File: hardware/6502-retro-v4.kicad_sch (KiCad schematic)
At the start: 51 parts, among them J1 SDCARD, J2 SPI BUS, J3 GPIO, J4 CTS, J5 RTS, J6 UART, J7 JOY1, J8 SPK/AMP, J9 USB-C Adapter, U1 W65C22NxP, U10 AS6C4008-55PCN, U11 74LS32, U12 VDP, U13 SN76489AN, U14 74LS244, U15 DS1813-5, U2 AT22V10, U3 W65C02SxP, U4 W65C22NxP, U5 74HC138, U6 27C512, U7 74HC273, U8 AS6C4008-55PCN, U9 6551, Y1 4MHz, Y2 1.8432MHz

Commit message: SN76489AN /SNWE signal needs to be driven by VIA
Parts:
- added R4: 2.2K, Resistor_THT:R_Axial_DIN0204_L3.6mm_D1.6mm_P5.08mm_Horizontal, symbol Device:R
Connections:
- net GND: now also U13.6 (~{CE})
- net SNREADY: now also R4.1
- net USRLED: now also U1.6 (PA4); no longer U1.7 (PA5)
- net VCC: now also R4.2
- net ~{MEMWE}: no longer U13.5 (~{WE})
- net ~{SNEN}: no longer names the net of U5.9 (~{Y6})
- net ~{SNEN}: no longer U13.6 (~{CE})
- net ~{SPICS4}: no longer names the net of J2.8 (Pin_8)
- net ~{SPICS4}: no longer U1.6 (PA4)
- new net ~{SNWE}: U1.7 (PA5), U13.5 (~{WE})
- no-connect marks 24 -> 26
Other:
- note added: "4.1: /SNWE ADDED USERLED MOVED TO PA4"
- note added: "4.1: /SNWE FROM VIA, ADD 2.2K PULLUP"
- note added: "4.1: /SPICS4 REMOVED TO ALLOW FOR /SNWE"
- moved on the sheet: J8

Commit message: fix usb-c power pins
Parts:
- U1, U4: value W65C22NxP -> W65C22S
- U10, U8: value AS6C4008-55PCN -> AS6C4008
- U3: value W65C02SxP -> W65C02S
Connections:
- net GND: now also J9.1 (Pin_1); no longer J9.4 (Pin_4)
- net VCC: now also J9.4 (Pin_4); no longer J9.1 (Pin_1)
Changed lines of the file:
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@@
 	(title_block
 		(title "6502-Retro!")
-		(date "2026-01-26")
-		(rev "4.1")
+		(date "2026-02-05")
+		(rev "4.2")
 	)
 	(text "Up"
@@
 	)
 	(junction
-		(at 382.27 33.02)
-		(diameter 0)
-		(color 0 0 0 0)
-	)
-	(junction
 		(at 355.6 204.47)
 		(diameter 0)
@@
 	)
 	(junction
-		(at 335.28 196.85)
+		(at 382.27 33.02)
 		(diameter 0)
 		(color 0 0 0 0)
 	)
 	(junction
-		(at 382.27 25.4)
+		(at 335.28 196.85)
 		(diameter 0)
 		(color 0 0 0 0)
@@
 	(wire
 		(pts
-			(xy 382.27 21.59) (xy 382.27 25.4)
+			(xy 382.27 21.59) (xy 382.27 22.86)
 		)
 		(stroke
@@
 			)
 		)
-		(property "Value" "W65C22NxP"
+		(property "Value" "W65C22S"
 			(at 89.7733 199.39 0)
 			(effects
@@
 			)
 		)
-		(property "Value" "W65C22NxP"
+		(property "Value" "W65C22S"
 			(at 40.2433 199.39 0)
 			(effects
@@
 			)
 		)
-		(property "Value" "AS6C4008-55PCN"
+		(property "Value" "AS6C4008"
 			(at 172.3233 38.1 0)
 			(effects
@@
 		(exclude_from_sim yes)
 		(in_bom no)
-		(on_board no)
+		(on_board yes)
 		(dnp no)
 		(fields_autoplaced yes)
@@
 			)
 		)
-		(property "Footprint" ""
+		(property "Footprint" "Symbol:OSHW-Logo_5.7x6mm_SilkScreen"
 			(at 330.2 233.68 0)
 			(effects
@@
 			)
 		)
-		(property "Value" "AS6C4008-55PCN"
+		(property "Value" "AS6C4008"
 			(at 214.2333 38.1 0)
 			(effects
@@
 	(symbol
 		(lib_id "Connector_Generic:Conn_01x04")
-		(at 387.35 27.94 0)
+		(at 387.35 30.48 0)
+		(mirror x)
 		(unit 1)
 		(exclude_from_sim no)
@@
 		(on_board yes)
 		(dnp no)
-		(fields_autoplaced yes)
 		(property "Reference" "J9"
-			(at 389.89 27.9399 0)
+			(at 389.89 30.4801 0)
 			(effects
 				(font
@@
 		)
 		(property "Value" "USB-C Adapter"
-			(at 389.89 30.4799 0)
+			(at 389.89 27.9401 0)
 			(effects
 				(font
@@
 		)
 		(property "Footprint" "Connector_PinSocket_2.54mm:PinSocket_1x04_P2.54mm_Vertical"
-			(at 387.35 27.94 0)
+			(at 387.35 30.48 0)
 			(effects
 				(font
@@
 		)
 		(property "Datasheet" "~"
-			(at 387.35 27.94 0)
+			(at 387.35 30.48 0)
 			(effects
 				(font
@@
 		)
 		(property "Description" "Generic connector, single row, 01x04, script generated (kicad-library-utils/schlib/autogen/connector/)"
-			(at 387.35 27.94 0)
+			(at 387.35 30.48 0)
 			(effects
 				(font
@@
 			)
 		)
-		(property "Value" "W65C02SxP"
+		(property "Value" "W65C02S"
 			(at 73.2633 30.48 0)
 			(effects

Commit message: Schematic updated to v4.3
- 2 bus expansion slots
- larger board
- GAL16v8 to OR together all IRQ
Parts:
- added C11, C16: 0.1uF, Capacitor_THT:C_Disc_D3.0mm_W2.0mm_P2.50mm, symbol Device:C
- added H1, H2, H3, H4: MountingHole_Pad, MountingHole:MountingHole_3.2mm_M3_Pad, symbol Mechanical:MountingHole_Pad
- added J11: EXP2, Connector_PinSocket_2.54mm:PinSocket_1x38_P2.54mm_Vertical, symbol Connector:Conn_01x38_Female
- added J9: EXP1, Connector_PinSocket_2.54mm:PinSocket_1x38_P2.54mm_Vertical, symbol Connector:Conn_01x38_Female
- added U7: GAL16V8, PCM_Package_DIP_AKL:DIP-20_W7.62mm_Socket, symbol Logic_Programmable:GAL16V8
- C1, C2: footprint Capacitor_THT:C_Disc_D3.0mm_W2.0mm_P2.50mm -> Capacitor_THT:C_Disc_D3.8mm_W2.6mm_P2.50mm
- renumbered C11 to C12, C12 to C13, C13 to C14, C14 to C15, C15 to C17, C16 to C18, C17 to C19, J9 to J10, R2 to R1, R1 to R2, R4 to R3, R3 to R4, U2 to U1, U9 to U10, U10 to U11, U11 to U12, U12 to U13, U13 to U14, U14 to U15, U15 to U16, U1 to U2, U5 to U4, U4 to U5, U7 to U9
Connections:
- net A0: now also J11.2 (Pin_2), J9.2 (Pin_2)
- net A1: now also J11.3 (Pin_3), J9.3 (Pin_3)
- net A10: now also J11.12 (Pin_12), J9.12 (Pin_12)
- net A11: now also J11.13 (Pin_13), J9.13 (Pin_13)
- net A12: now also J11.14 (Pin_14), J9.14 (Pin_14)
- net A13: now also J11.15 (Pin_15), J9.15 (Pin_15)
- net A14: now also J11.16 (Pin_16), J9.16 (Pin_16)
- net A15: now also J11.17 (Pin_17), J9.17 (Pin_17)
- net A2: now also J11.4 (Pin_4), J9.4 (Pin_4)
- net A3: now also J11.5 (Pin_5), J9.5 (Pin_5)
- net A4: now also J11.6 (Pin_6), J9.6 (Pin_6)
- net A5: now also J11.7 (Pin_7), J9.7 (Pin_7)
- net A6: now also J11.8 (Pin_8), J9.8 (Pin_8)
- net A7: now also U1.11 (IN), J11.9 (Pin_9), J9.9 (Pin_9)
- net A8: now also J11.10 (Pin_10), J9.10 (Pin_10)
- net A9: now also J11.11 (Pin_11), J9.11 (Pin_11)
- net BE: now also J11.37 (Pin_37), J9.37 (Pin_37)
- net D0: now also J11.20 (Pin_20), J9.20 (Pin_20)
- net D1: now also J11.21 (Pin_21), J9.21 (Pin_21)
- net D2: now also J11.22 (Pin_22), J9.22 (Pin_22)
- net D3: now also J11.23 (Pin_23), J9.23 (Pin_23)
- net D4: now also J11.24 (Pin_24), J9.24 (Pin_24)
- net D5: now also J11.25 (Pin_25), J9.25 (Pin_25)
- net D6: now also J11.26 (Pin_26), J9.26 (Pin_26)
- net D7: now also J11.27 (Pin_27), J9.27 (Pin_27)
- net GND: now also R1.1, C11.1, C16.1, H1.1, H2.1, H3.1, H4.1, J11.1 (Pin_1), J11.18 (Pin_18), J11.38 (Pin_38), J9.1 (Pin_1), J9.18 (Pin_18), J9.38 (Pin_38), U7.10 (GND)
- net PHI2: now also J11.28 (Pin_28), J9.28 (Pin_28)
- net RDY: now also J11.36 (Pin_36), J9.36 (Pin_36)
- net R/~{W}: now also J11.29 (Pin_29), J9.29 (Pin_29)
- net USRLED: now also D1.2 (A); no longer R1.1
- net VCC: now also C11.2, C16.2, J11.19 (Pin_19), J9.19 (Pin_19), U7.20 (VCC); no longer D1.2 (A)
- net ~{ACIAIRQ}: now also U7.2 (I2); no longer U1.11 (IN)
- net ~{IRQ}: now also U7.19 (IO1); no longer U1.23 (I/O)
- net ~{MEMOE}: now also U1.16 (I/O); no longer U1.17 (I/O)
- net ~{MEMWE}: now also U1.15 (I/O); no longer U1.16 (I/O)
- net ~{NMI}: now also J11.35 (Pin_35), J9.35 (Pin_35)
- net ~{RST}: now also J11.33 (Pin_33), J9.33 (Pin_33)
- net ~{VDPIRQ}: now also U7.5 (I5); no longer RN1.7 (R6), U1.15 (I/O)
- net ~{VIA1IRQ}: now also U7.3 (I3); no longer U1.13 (IN)
- net ~{VIA2IRQ}: now also U7.4 (I4); no longer U1.14 (I/O)
- net ~{IOEXP2}: now reaches U4.7 (~{Y7})
- net ~{IOEXP2}: now also J11.31 (Pin_31), J9.31 (Pin_31)
- net ~{IOEXP1}: now reaches U4.9 (~{Y6})
- net ~{IOEXP1}: now also J11.32 (Pin_32), J9.32 (Pin_32)
- net ~{IOCS} renamed ~{IOCSL}
- new net ~{IOCSH}: J11.30 (Pin_30), J9.30 (Pin_30), U1.17 (I/O)
- new net ~{IRQEXP1}: J9.34 (Pin_34), U7.6 (I6)
- new net ~{IRQEXP2}: J11.34 (Pin_34), U7.7 (I7)
- no-connect marks 26 -> 39
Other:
- note added: "BUS PLD"
- note added: "IRQ COMBINER"
- note removed: "BUS & IRQ"
- moved on the sheet: D1, J7, J8, R1, R2, R3, RN2, U1, U14, U15, U4, U9

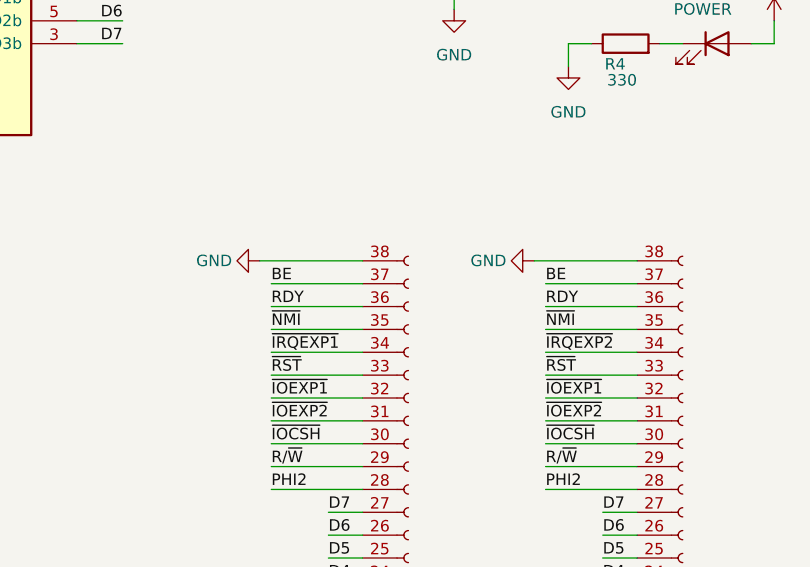
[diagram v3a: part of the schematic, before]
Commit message: Add resistors to expansion slot IRQ pins
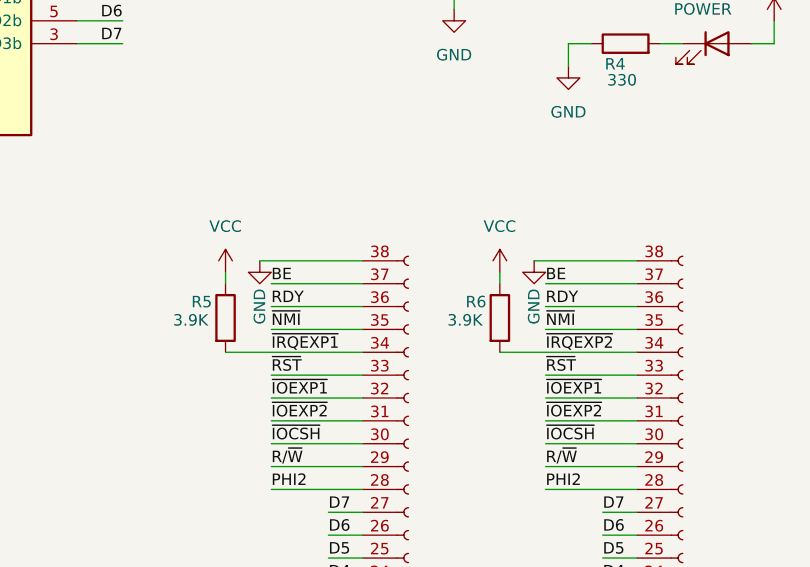
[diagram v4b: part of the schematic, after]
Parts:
- added R5, R6: 3.9K, Resistor_THT:R_Axial_DIN0204_L3.6mm_D1.6mm_P5.08mm_Horizontal, symbol Device:R
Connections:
- net VCC: now also R5.1, R6.1
- net ~{IRQEXP1}: now also R5.2
- net ~{IRQEXP2}: now also R6.2
